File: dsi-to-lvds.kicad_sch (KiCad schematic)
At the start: 22 parts, among them U2 NTS0104_DHVQFN, U3 SN65DSI84

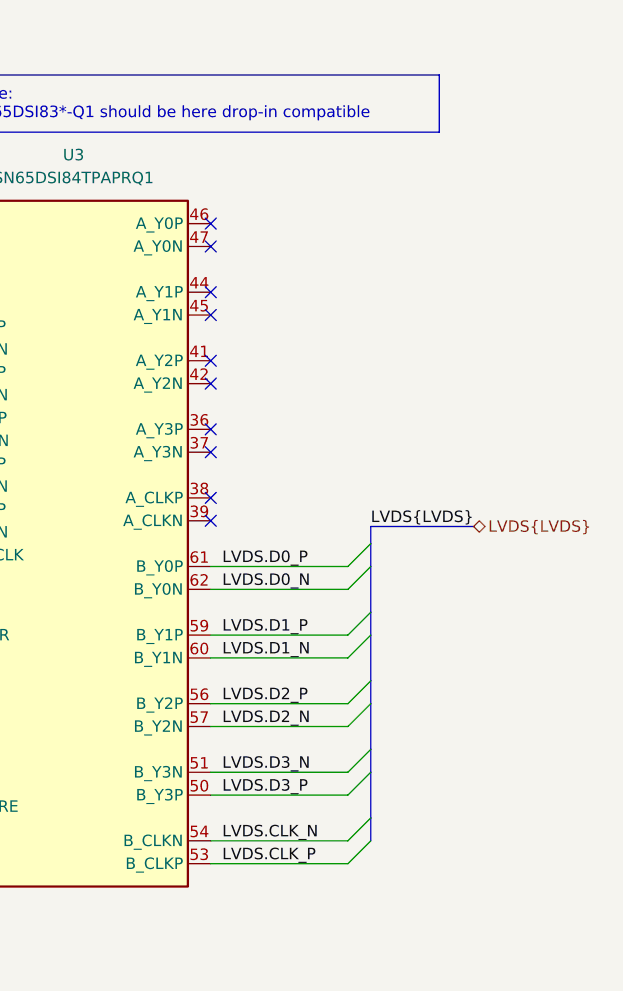
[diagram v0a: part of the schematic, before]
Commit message: [#58357] SN65DSI84: use channel A instead of CH-B
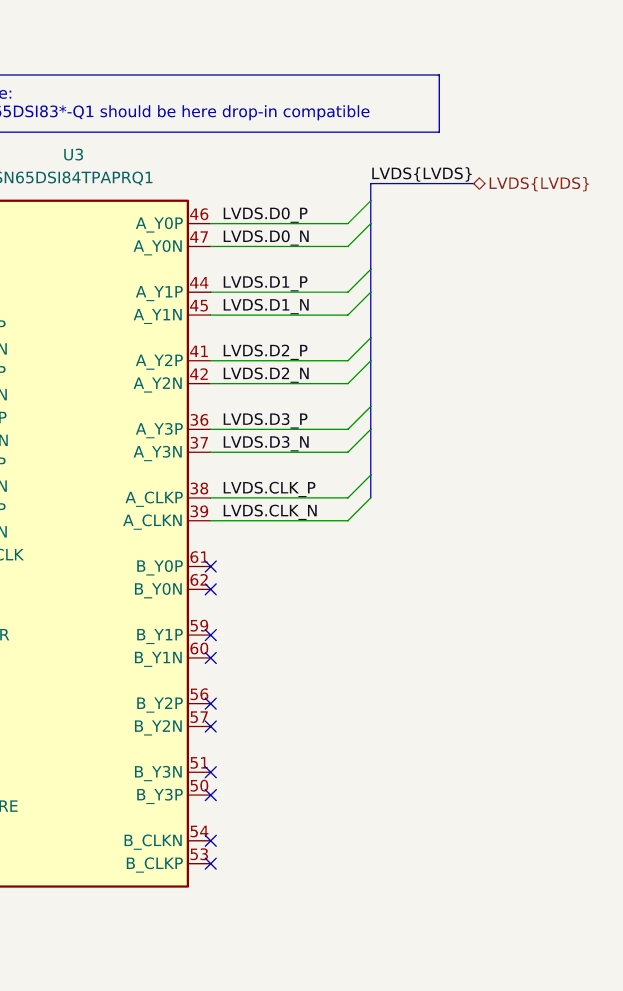
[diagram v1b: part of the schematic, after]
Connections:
- net LVDS.CLK_N: now also U3.39 (A_CLKN); no longer U3.54 (B_CLKN)
- net LVDS.CLK_P: now also U3.38 (A_CLKP); no longer U3.53 (B_CLKP)
- net LVDS.D0_N: now also U3.47 (A_Y0N); no longer U3.62 (B_Y0N)
- net LVDS.D0_P: now also U3.46 (A_Y0P); no longer U3.61 (B_Y0P)
- net LVDS.D1_N: now also U3.45 (A_Y1N); no longer U3.60 (B_Y1N)
- net LVDS.D1_P: now also U3.44 (A_Y1P); no longer U3.59 (B_Y1P)
- net LVDS.D2_N: now also U3.42 (A_Y2N); no longer U3.57 (B_Y2N)
- net LVDS.D2_P: now also U3.41 (A_Y2P); no longer U3.56 (B_Y2P)
- net LVDS.D3_N: now also U3.37 (A_Y3N); no longer U3.51 (B_Y3N)
- net LVDS.D3_P: now also U3.36 (A_Y3P); no longer U3.50 (B_Y3P)
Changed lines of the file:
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@@
   (junction (at 123.19 52.07) (diameter 0) (color 0 0 0 0)
   )
-  (no_connect (at 223.52 95.25))
-  (no_connect (at 223.52 74.93))
-  (no_connect (at 223.52 87.63))
-  (no_connect (at 223.52 97.79))
-  (no_connect (at 223.52 67.31))
-  (no_connect (at 223.52 64.77))
-  (no_connect (at 223.52 82.55))
-  (no_connect (at 223.52 80.01))
-  (no_connect (at 223.52 72.39))
-  (no_connect (at 223.52 90.17))
+  (no_connect (at 223.52 133.35))
+  (no_connect (at 223.52 113.03))
+  (no_connect (at 223.52 125.73))
+  (no_connect (at 223.52 135.89))
+  (no_connect (at 223.52 105.41))
+  (no_connect (at 223.52 102.87))
+  (no_connect (at 223.52 120.65))
+  (no_connect (at 223.52 118.11))
+  (no_connect (at 223.52 110.49))
+  (no_connect (at 223.52 128.27))
   (bus_entry (at 173.99 85.09) (size 1.27 1.27)
     (stroke (width 0) (type default))
@@
     (stroke (width 0) (type default))
   )
-  (bus_entry (at 241.3 110.49) (size -2.54 2.54)
+  (bus_entry (at 241.3 72.39) (size -2.54 2.54)
     (stroke (width 0) (type default))
   )
@@
     (stroke (width 0) (type default))
   )
-  (bus_entry (at 241.3 123.19) (size -2.54 2.54)
-    (stroke (width 0) (type default))
-  )
-  (bus_entry (at 241.3 100.33) (size -2.54 2.54)
+  (bus_entry (at 241.3 85.09) (size -2.54 2.54)
+    (stroke (width 0) (type default))
+  )
+  (bus_entry (at 241.3 62.23) (size -2.54 2.54)
     (stroke (width 0) (type default))
   )
@@
     (stroke (width 0) (type default))
   )
-  (bus_entry (at 241.3 102.87) (size -2.54 2.54)
-    (stroke (width 0) (type default))
-  )
-  (bus_entry (at 241.3 118.11) (size -2.54 2.54)
+  (bus_entry (at 241.3 64.77) (size -2.54 2.54)
+    (stroke (width 0) (type default))
+  )
+  (bus_entry (at 241.3 80.01) (size -2.54 2.54)
     (stroke (width 0) (type default))
   )
@@
     (stroke (width 0) (type default))
   )
-  (bus_entry (at 241.3 130.81) (size -2.54 2.54)
+  (bus_entry (at 241.3 92.71) (size -2.54 2.54)
     (stroke (width 0) (type default))
   )
@@
     (stroke (width 0) (type default))
   )
-  (bus_entry (at 241.3 115.57) (size -2.54 2.54)
-    (stroke (width 0) (type default))
-  )
-  (bus_entry (at 238.76 135.89) (size 2.54 -2.54)
-    (stroke (width 0) (type default))
-  )
-  (bus_entry (at 241.3 107.95) (size -2.54 2.54)
+  (bus_entry (at 241.3 77.47) (size -2.54 2.54)
+    (stroke (width 0) (type default))
+  )
+  (bus_entry (at 238.76 97.79) (size 2.54 -2.54)
+    (stroke (width 0) (type default))
+  )
+  (bus_entry (at 241.3 69.85) (size -2.54 2.54)
     (stroke (width 0) (type default))
   )
@@
     (stroke (width 0) (type default))
   )
-  (bus_entry (at 241.3 125.73) (size -2.54 2.54)
+  (bus_entry (at 241.3 87.63) (size -2.54 2.54)
     (stroke (width 0) (type default))
   )
@@
     (stroke (width 0) (type default))
   )
-  (wire (pts (xy 223.52 105.41) (xy 238.76 105.41))
+  (wire (pts (xy 223.52 67.31) (xy 238.76 67.31))
     (stroke (width 0) (type default))
   )
@@
     (stroke (width 0) (type default))
   )
-  (bus (pts (xy 241.3 125.73) (xy 241.3 130.81))
+  (bus (pts (xy 241.3 87.63) (xy 241.3 92.71))
     (stroke (width 0) (type default))
   )
@@
     (stroke (width 0) (type default))
   )
-  (wire (pts (xy 223.52 135.89) (xy 238.76 135.89))
+  (wire (pts (xy 223.52 97.79) (xy 238.76 97.79))
     (stroke (width 0) (type default))
   )
@@
     (stroke (width 0) (type default))
   )
-  (wire (pts (xy 223.52 102.87) (xy 238.76 102.87))
+  (wire (pts (xy 223.52 64.77) (xy 238.76 64.77))
     (stroke (width 0) (type default))
   )
@@
     (stroke (width 0) (type default))
   )
-  (bus (pts (xy 241.3 102.87) (xy 241.3 107.95))
+  (bus (pts (xy 241.3 64.77) (xy 241.3 69.85))
     (stroke (width 0) (type default))
   )
@@
     (stroke (width 0) (type default))
   )
-  (bus (pts (xy 241.3 98.425) (xy 241.3 100.33))
-    (stroke (width 0) (type default))
-  )
-  (bus (pts (xy 241.3 100.33) (xy 241.3 102.87))
-    (stroke (width 0) (type default))
-  )
-  (wire (pts (xy 223.52 110.49) (xy 238.76 110.49))
+  (bus (pts (xy 241.3 60.325) (xy 241.3 62.23))
+    (stroke (width 0) (type default))
+  )
+  (bus (pts (xy 241.3 62.23) (xy 241.3 64.77))
+    (stroke (width 0) (type default))
+  )
+  (wire (pts (xy 223.52 72.39) (xy 238.76 72.39))
     (stroke (width 0) (type default))
   )
@@
     (stroke (width 0) (type default))
   )
-  (wire (pts (xy 223.52 128.27) (xy 238.76 128.27))
+  (wire (pts (xy 223.52 90.17) (xy 238.76 90.17))
     (stroke (width 0) (type default))
   )
@@
     (stroke (width 0) (type default))
   )
-  (bus (pts (xy 241.3 130.81) (xy 241.3 133.35))
+  (bus (pts (xy 241.3 92.71) (xy 241.3 95.25))
     (stroke (width 0) (type default))
   )
@@
     (stroke (width 0) (type default))
   )
-  (bus (pts (xy 252.73 98.425) (xy 241.3 98.425))
+  (bus (pts (xy 252.73 60.325) (xy 241.3 60.325))
     (stroke (width 0) (type default))
   )
@@
     (stroke (width 0) (type default))
   )
-  (bus (pts (xy 241.3 118.11) (xy 241.3 123.19))
+  (bus (pts (xy 241.3 80.01) (xy 241.3 85.09))
     (stroke (width 0) (type default))
   )
@@
     (stroke (width 0) (type default))
   )
-  (wire (pts (xy 223.52 118.11) (xy 238.76 118.11))
+  (wire (pts (xy 223.52 80.01) (xy 238.76 80.01))
     (stroke (width 0) (type default))
   )
@@
     (stroke (width 0) (type default))
   )
-  (bus (pts (xy 241.3 115.57) (xy 241.3 118.11))
+  (bus (pts (xy 241.3 77.47) (xy 241.3 80.01))
     (stroke (width 0) (type default))
   )
@@
     (stroke (width 0) (type default))
   )
-  (wire (pts (xy 223.52 125.73) (xy 238.76 125.73))
+  (wire (pts (xy 223.52 87.63) (xy 238.76 87.63))
     (stroke (width 0) (type default))
   )
@@
     (stroke (width 0) (type default))
   )
-  (bus (pts (xy 241.3 107.95) (xy 241.3 110.49))
+  (bus (pts (xy 241.3 69.85) (xy 241.3 72.39))
     (stroke (width 0) (type default))
   )
@@
     (stroke (width 0) (type default))
   )
-  (bus (pts (xy 241.3 123.19) (xy 241.3 125.73))
+  (bus (pts (xy 241.3 85.09) (xy 241.3 87.63))
     (stroke (width 0) (type default))
   )
@@
     (stroke (width 0) (type default))
   )
-  (wire (pts (xy 223.52 120.65) (xy 238.76 120.65))
+  (wire (pts (xy 223.52 82.55) (xy 238.76 82.55))
     (stroke (width 0) (type default))
   )
@@
     (stroke (width 0) (type default))
   )
-  (wire (pts (xy 223.52 133.35) (xy 238.76 133.35))
+  (wire (pts (xy 223.52 95.25) (xy 238.76 95.25))
     (stroke (width 0) (type default))
   )
@@
     (stroke (width 0) (type default))
   )
-  (wire (pts (xy 223.52 113.03) (xy 238.76 113.03))
+  (wire (pts (xy 223.52 74.93) (xy 238.76 74.93))
     (stroke (width 0) (type default))
   )
@@
     (stroke (width 0) (type default))
   )
-  (bus (pts (xy 241.3 110.49) (xy 241.3 115.57))
+  (bus (pts (xy 241.3 72.39) (xy 241.3 77.47))
     (stroke (width 0) (type default))
   )
@@
     (effects (font (size 1.27 1.27)) (justify left bottom))
   )
-  (label "LVDS.D1_P" (at 224.79 110.49 0) (fields_autoplaced)
-    (effects (font (size 1.27 1.27)) (justify left bottom))
-  )
-  (label "LVDS.D3_N" (at 224.79 125.73 0) (fields_autoplaced)
+  (label "LVDS.D1_P" (at 224.79 72.39 0) (fields_autoplaced)
+    (effects (font (size 1.27 1.27)) (justify left bottom))
+  )
+  (label "LVDS.D3_N" (at 224.79 90.17 0) (fields_autoplaced)
     (effects (font (size 1.27 1.27)) (justify left bottom))
   )
@@
     (effects (font (size 1.27 1.27)) (justify left bottom))
   )
-  (label "LVDS.D0_N" (at 224.79 105.41 0) (fields_autoplaced)
+  (label "LVDS.D0_N" (at 224.79 67.31 0) (fields_autoplaced)
     (effects (font (size 1.27 1.27)) (justify left bottom))
   )
@@
     (effects (font (size 1.27 1.27)) (justify left bottom))
   )
-  (label "LVDS.D3_P" (at 224.79 128.27 0) (fields_autoplaced)
-    (effects (font (size 1.27 1.27)) (justify left bottom))
-  )
-  (label "LVDS.CLK_N" (at 224.79 133.35 0) (fields_autoplaced)
+  (label "LVDS.D3_P" (at 224.79 87.63 0) (fields_autoplaced)
+    (effects (font (size 1.27 1.27)) (justify left bottom))
+  )
+  (label "LVDS.CLK_N" (at 224.79 97.79 0) (fields_autoplaced)
     (effects (font (size 1.27 1.27)) (justify left bottom))
   )
@@
     (effects (font (size 1.27 1.27)) (justify left bottom))
   )
-  (label "LVDS.D1_N" (at 224.79 113.03 0) (fields_autoplaced)
+  (label "LVDS.D1_N" (at 224.79 74.93 0) (fields_autoplaced)
     (effects (font (size 1.27 1.27)) (justify left bottom))
   )
@@
     (effects (font (size 1.27 1.27)) (justify left bottom))
   )
-  (label "LVDS{LVDS}" (at 252.73 98.425 180) (fields_autoplaced)
+  (label "LVDS{LVDS}" (at 252.73 60.325 180) (fields_autoplaced)
     (effects (font (size 1.27 1.27)) (justify right bottom))
   )
@@
     (effects (font (size 1.27 1.27)) (justify left bottom))
   )
-  (label "LVDS.D2_P" (at 224.79 118.11 0) (fields_autoplaced)
+  (label "LVDS.D2_P" (at 224.79 80.01 0) (fields_autoplaced)
     (effects (font (size 1.27 1.27)) (justify left bottom))
   )
@@
     (effects (font (size 1.27 1.27)) (justify left bottom))
   )
-  (label "LVDS.D2_N" (at 224.79 120.65 0) (fields_autoplaced)
+  (label "LVDS.D2_N" (at 224.79 82.55 0) (fields_autoplaced)
     (effects (font (size 1.27 1.27)) (justify left bottom))
   )
@@
     (effects (font (size 1.27 1.27)) (justify left bottom))
   )
-  (label "LVDS.D0_P" (at 224.79 102.87 0) (fields_autoplaced)
-    (effects (font (size 1.27 1.27)) (justify left bottom))
-  )
-  (label "LVDS.CLK_P" (at 224.79 135.89 0) (fields_autoplaced)
+  (label "LVDS.D0_P" (at 224.79 64.77 0) (fields_autoplaced)
+    (effects (font (size 1.27 1.27)) (justify left bottom))
+  )
+  (label "LVDS.CLK_P" (at 224.79 95.25 0) (fields_autoplaced)
     (effects (font (size 1.27 1.27)) (justify left bottom))
   )
@@
     (effects (font (size 1.27 1.27)) (justify left bottom))
   )
-  (hierarchical_label "LVDS{LVDS}" (shape bidirectional) (at 252.73 98.425 0) (fields_autoplaced)
+  (hierarchical_label "LVDS{LVDS}" (shape bidirectional) (at 252.73 60.325 0) (fields_autoplaced)
     (effects (font (size 1.27 1.27)) (justify left))
   )

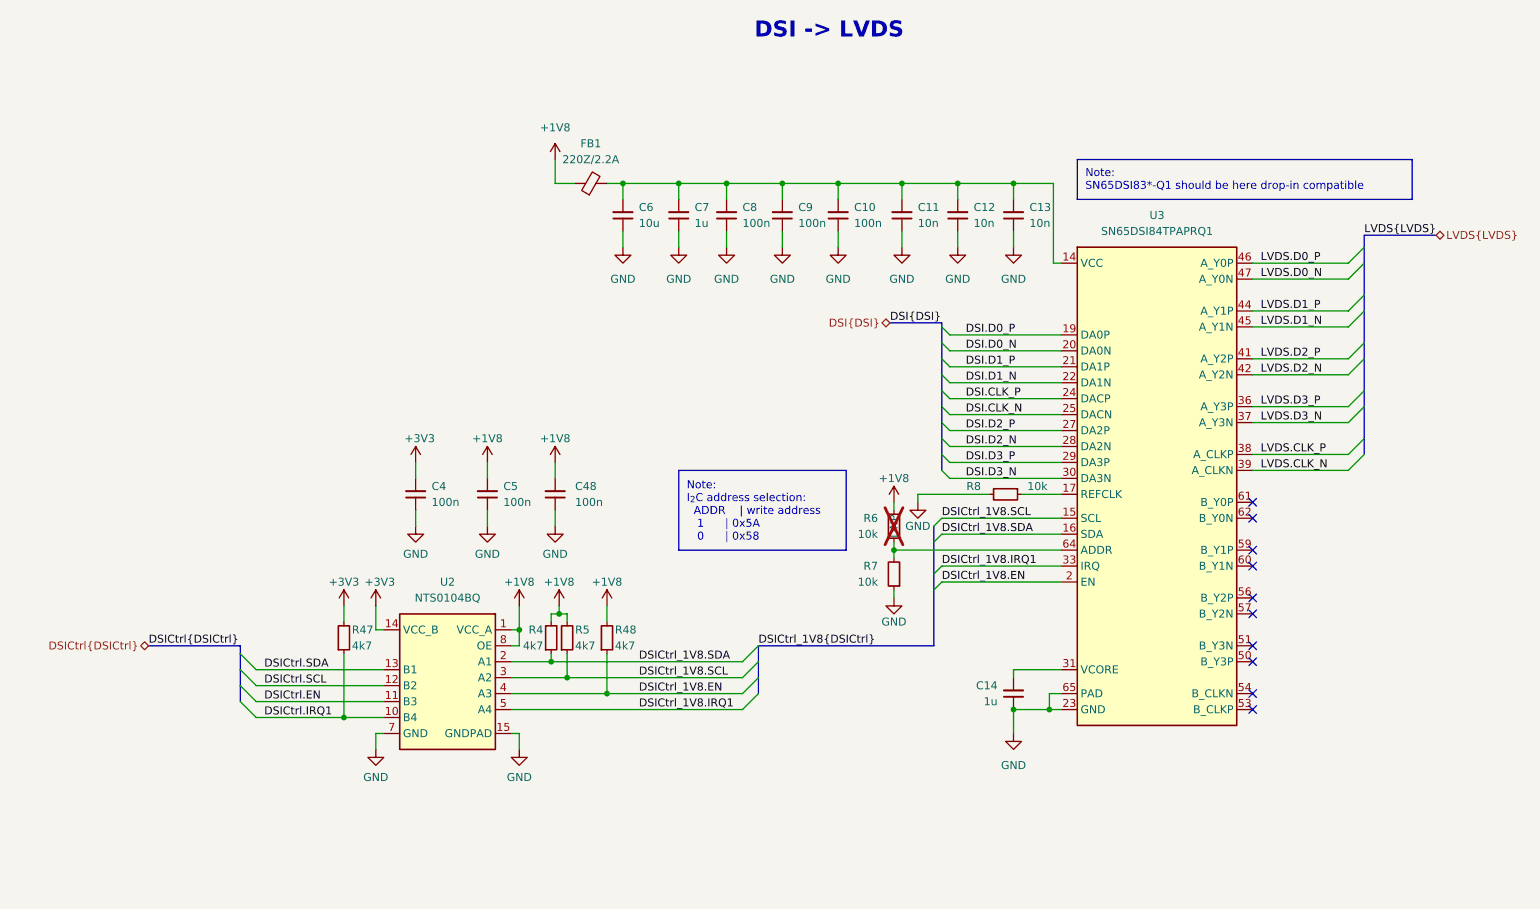
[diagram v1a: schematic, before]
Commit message: [#58358] SN65DSI84: Fix IRQ1 line
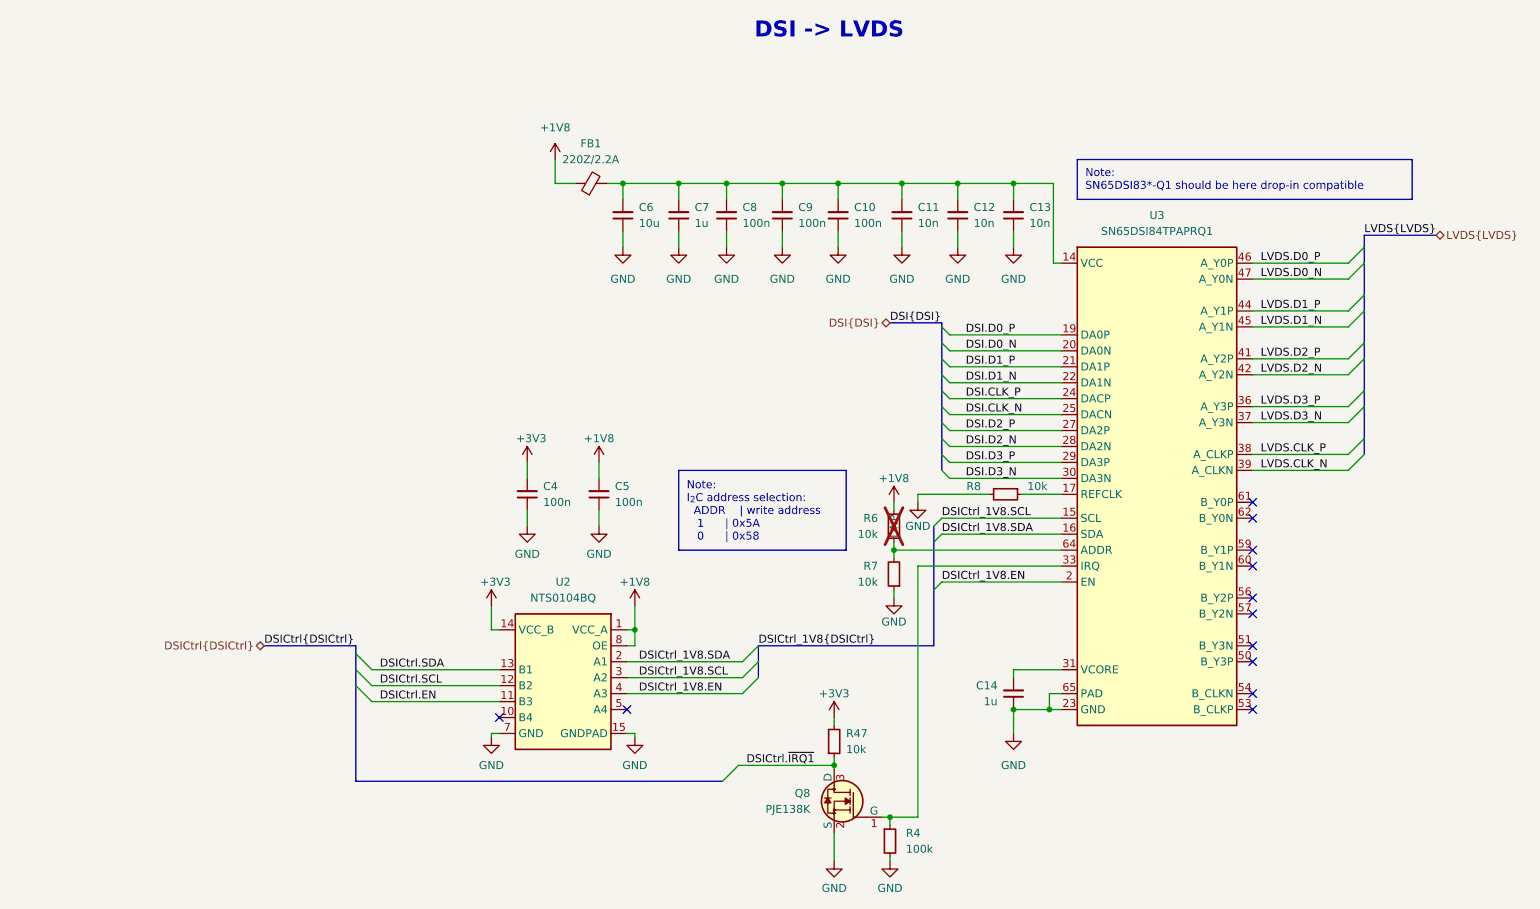
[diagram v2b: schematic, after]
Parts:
- removed C48: C_100n_0402, antmicro-footprints:C_0402_1005Metric, symbol antmicroCapacitors0402:C_100n_0402
- removed R4, R48, R5: R_4k7_0402, antmicro-footprints:R_0402_1005Metric, symbol antmicroResistors0402:R_4k7_0402
- added Q8: PJE138K, antmicro-footprints:SOT-523, symbol antmicroTransistorsFETsMOSFETsSingle:PJE138K
- added R4: R_100k_0402, antmicro-footprints:R_0402_1005Metric, symbol antmicroResistors0402:R_100k_0402
- R47: value R_4k7_0402 -> R_10k_0402; symbol antmicroResistors0402:R_4k7_0402 -> antmicroResistors0402:R_10k_0402; MPN CR0402-FX-4701GLF -> CR0402-FX-1002GLF; Val 4k7 -> 10k
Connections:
- net GND: now also Q8.2 (S), R4.2
- net DSICtrl.IRQ1: no longer names the net of U2.10 (B4)
- net DSICtrl.IRQ1: no longer R47.1
- net DSICtrl_1V8.IRQ1: no longer names the net of U3.33 (IRQ)
- net DSICtrl_1V8.IRQ1: now also Q8.1 (G), R4.1; no longer U2.5 (A4)
- new net DSICtrl.~{IRQ1}: Q8.3 (D), R47.1
- no-connect marks 10 -> 12
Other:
- moved on the sheet: C4, C5, R47, U2
